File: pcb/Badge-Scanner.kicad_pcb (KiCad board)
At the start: 2 copper layers, 73 x 52 mm, 64 parts, among them J1 NFC-Module, J2 Serial, J3 I2C, J4 Micro_SD_Card_Det1, Q1 AO3400A, Q2 AO3401A, Q3 AO3401A, Q4 AO3401A, Q5 AO3400A, Q6 AO3400A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

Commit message: style: enlarge pin description text
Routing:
- net GND: vias 0 -> 3
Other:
- board text added: "SD-Card (SPI1) 11<DET 12<MISO 13>CS 14<SCK 15>MOSI NFC (SPI0) 16<MISO 17>CS 18>SCK 19>MOSI 20>RST 21<IRQ"
- board text removed: "SD-Card SPI1 11 DETECT 12 MISO 13 CS 14 SCK 15 MOSI NFC SPI0 16 MISO 17 CS 18 SCK 19 MOSI 20 RST 21 IRQ"
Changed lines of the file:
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@@
 	)
 	(gr_text " 0>UART0 TX\n 1<UART0 RX\n 2>LED\n 3>Buzzer\n 4=I2C0 SDA\n 5>I2C0 SCL\n 6<~{Button}\n 8<~{Charge Active}\n 9<~{Charge Standby}\n27>Power Off\n28<Battery Voltage	"
-		(at 164.5 115.75 0)
+		(at 165 118.5 0)
 		(layer "B.SilkS")
 		(effects
 			(font
-				(size 1 1)
+				(size 1.4 1.5)
 				(thickness 0.15)
 			)
@@
 		)
 	)
-	(gr_text "SD-Card SPI1\n11	DETECT\n12	MISO\n13	CS\n14	SCK\n15	MOSI\n\nNFC SPI0\n16	MISO\n17	CS\n18	SCK\n19	MOSI\n20	RST\n21	IRQ"
-		(at 105 115.75 0)
+	(gr_text "SD-Card\n(SPI1)\n11<DET\n12<MISO\n13>CS\n14<SCK\n15>MOSI\n\nNFC \n(SPI0)\n16<MISO\n17>CS\n18>SCK\n19>MOSI\n20>RST\n21<IRQ"
+		(at 104.75 118 0)
 		(layer "B.SilkS")
 		(effects
 			(font
-				(size 1 1)
+				(size 1.4 1.5)
 				(thickness 0.15)
 			)
@@
 		(net 7)
 	)
+	(via
+		(at 120 116.25)
+		(size 0.5)
+		(drill 0.3)
+		(layers "F.Cu" "B.Cu")
+		(free yes)
+		(net 7)
+	)
+	(via
+		(at 130 116.25)
+		(size 0.5)
+		(drill 0.3)
+		(layers "F.Cu" "B.Cu")
+		(free yes)
+		(net 7)
+	)
+	(via
+		(at 125 116.25)
+		(size 0.5)
+		(drill 0.3)
+		(layers "F.Cu" "B.Cu")
+		(free yes)
+		(net 7)
+	)

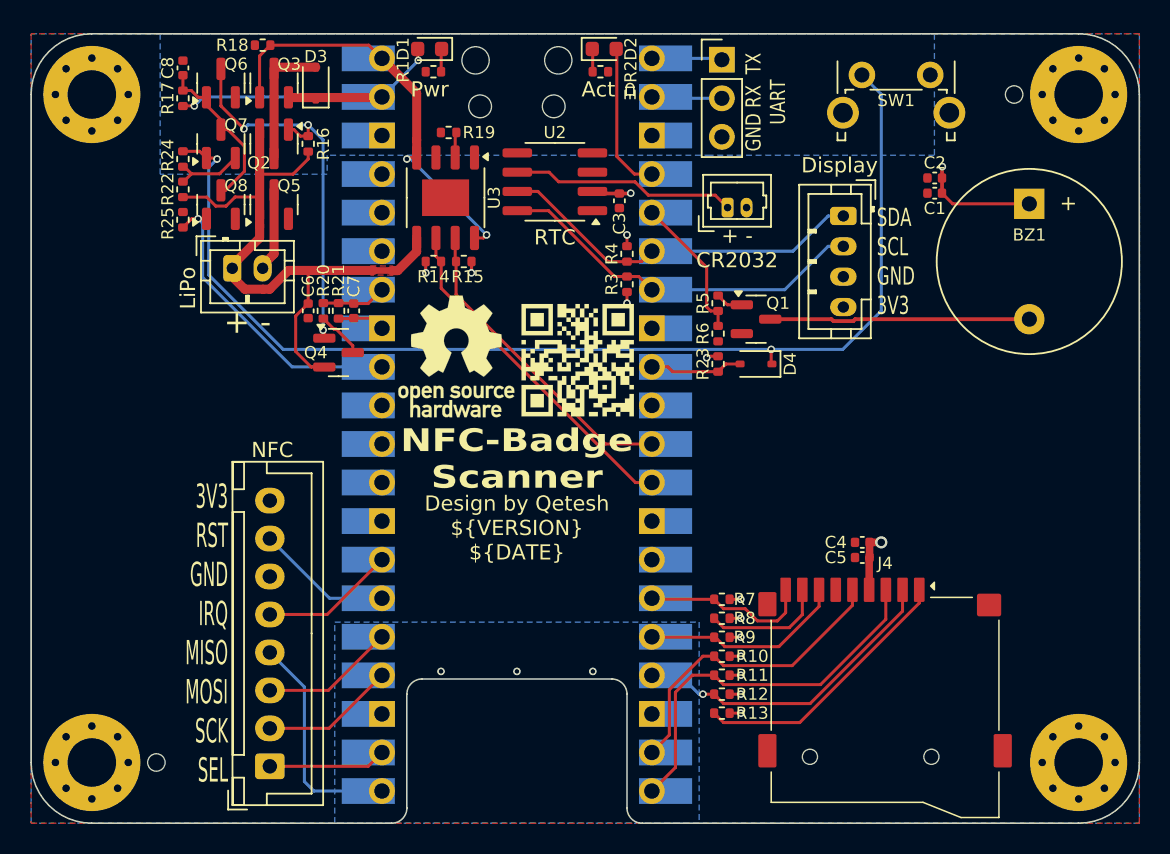
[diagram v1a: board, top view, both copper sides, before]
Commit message: style: silkscreen improvements
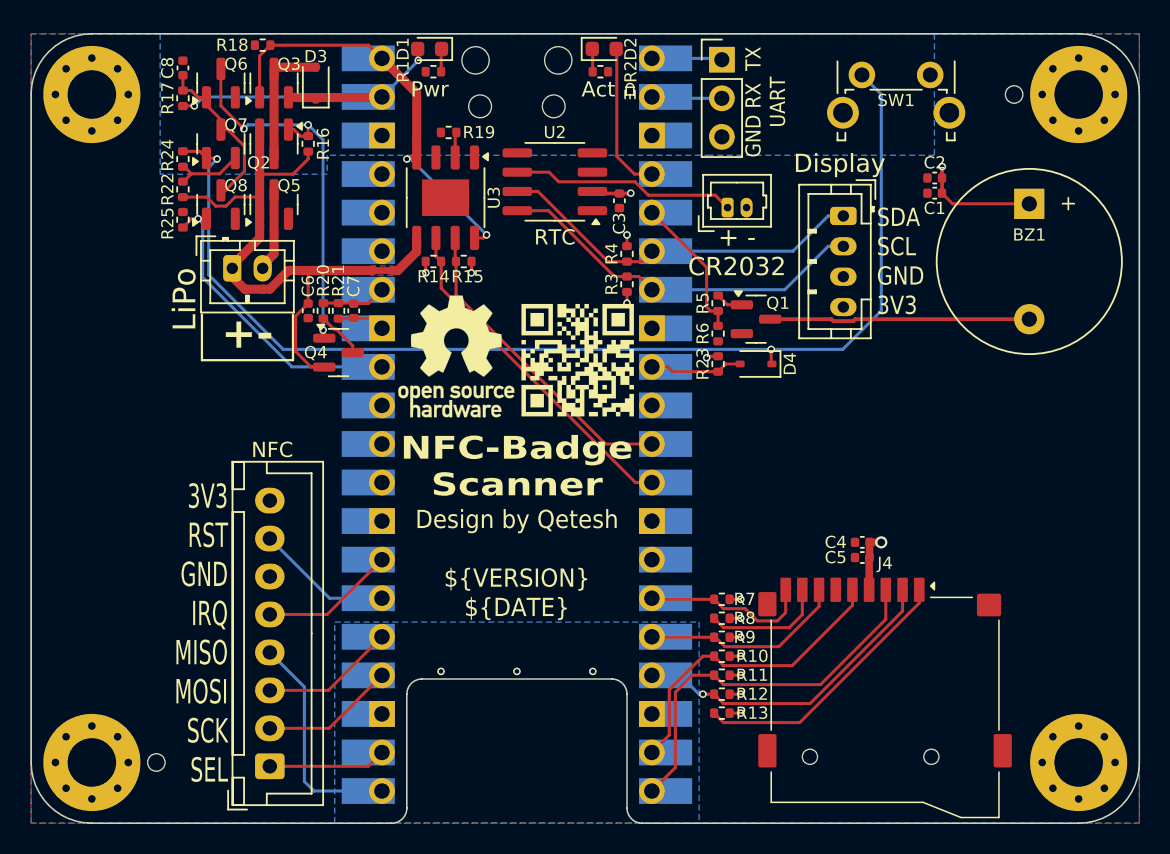
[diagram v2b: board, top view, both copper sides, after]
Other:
- board text added: "+-"
- board text removed: "+ -"
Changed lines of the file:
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@@
 	)
 	(setup
+		(stackup
+			(layer "F.SilkS"
+				(type "Top Silk Screen")
+				(color "White")
+			)
+			(layer "F.Paste"
+				(type "Top Solder Paste")
+			)
+			(layer "F.Mask"
+				(type "Top Solder Mask")
+				(color "Blue")
+				(thickness 0.01)
+			)
+			(layer "F.Cu"
+				(type "copper")
+				(thickness 0.035)
+			)
+			(layer "dielectric 1"
+				(type "core")
+				(color "FR4 natural")
+				(thickness 1.51)
+				(material "FR4")
+				(epsilon_r 4.5)
+				(loss_tangent 0.02)
+			)
+			(layer "B.Cu"
+				(type "copper")
+				(thickness 0.035)
+			)
+			(layer "B.Mask"
+				(type "Bottom Solder Mask")
+				(color "Blue")
+				(thickness 0.01)
+			)
+			(layer "B.Paste"
+				(type "Bottom Solder Paste")
+			)
+			(layer "B.SilkS"
+				(type "Bottom Silk Screen")
+				(color "White")
+			)
+			(copper_finish "None")
+			(dielectric_constraints no)
+		)
 		(pad_to_mask_clearance 0)
 		(allow_soldermask_bridges_in_footprints no)
@@
 		)
 	)
+	(gr_line
+		(start 110.25 95.75)
+		(end 110.25 92.75)
+		(stroke
+			(width 0.15)
+			(type default)
+		)
+		(layer "F.SilkS")
+	)
 	(gr_rect
 		(start 132.2 77.775)
@@
 	)
 	(gr_line
+		(start 104.25 92.75)
+		(end 104.25 95.75)
+		(stroke
+			(width 0.15)
+			(type default)
+		)
+		(layer "F.SilkS")
+	)
+	(gr_line
 		(start 132.125 77.975)
 		(end 132.125 78.525)
@@
 	)
 	(gr_line
+		(start 104.25 95.75)
+		(end 110.25 95.75)
+		(stroke
+			(width 0.15)
+			(type default)
+		)
+		(layer "F.SilkS")
+	)
+	(gr_line
 		(start 97 74.25)
 		(end 162 74.25)
@@
 		(effects
 			(font
-				(size 1 1)
+				(size 1.2 1.2)
 				(thickness 0.15)
 			)
@@
 		(effects
 			(font
-				(size 1.2 0.8)
+				(size 1.2 1)
 				(thickness 0.15)
 			)
@@
 		(effects
 			(font
-				(size 1.6 0.8)
+				(size 1.6 1)
 				(thickness 0.15)
 			)
@@
 		)
 	)
-	(gr_text "+ -"
-		(at 107.25 93.25 0)
+	(gr_text "+-"
+		(at 107.25 94 0)
 		(layer "F.SilkS")
 		(effects
 			(font
-				(size 1.5 1.5)
-				(thickness 0.2)
+				(size 2 2)
+				(thickness 0.4)
+				(bold yes)
 			)
 		)
 	)
-	(gr_text "Design by Qetesh\n${VERSION}\n${DATE}"
-		(at 125 109 0)
+	(gr_text "Design by Qetesh\n\n${VERSION}\n${DATE}"
+		(at 125 112.75 0)
 		(layer "F.SilkS")
 		(effects
 			(font
-				(size 1 1)
+				(size 1.2 1.1)
 				(thickness 0.15)
 			)
@@
 	)
 	(gr_text "+ -\nCR2032"
-		(at 139.5 89.75 0)
+		(at 139.5 86.96 0)
 		(layer "F.SilkS")
 		(effects
 			(font
-				(size 1 1)
+				(size 1.2 1.2)
 				(thickness 0.15)
 			)
-			(justify bottom)
+			(justify top)
 		)
 	)
@@
 		(effects
 			(font
-				(size 1 0.8)
+				(size 1 0.9)
 				(thickness 0.15)
 			)
@@
 	)
 	(gr_text "LiPo"
-		(at 102.75 91 90)
+		(at 104 91.75 90)
 		(layer "F.SilkS")
 		(effects
 			(font
-				(size 1 1)
+				(size 1.5 1.5)
 				(thickness 0.15)
 			)
-			(justify top)
+			(justify bottom)
 		)
 	)
 	(gr_text "NFC-Badge\nScanner"
-		(at 125 102.25 0)
+		(at 125 102.75 0)
 		(layer "F.SilkS")
 		(effects

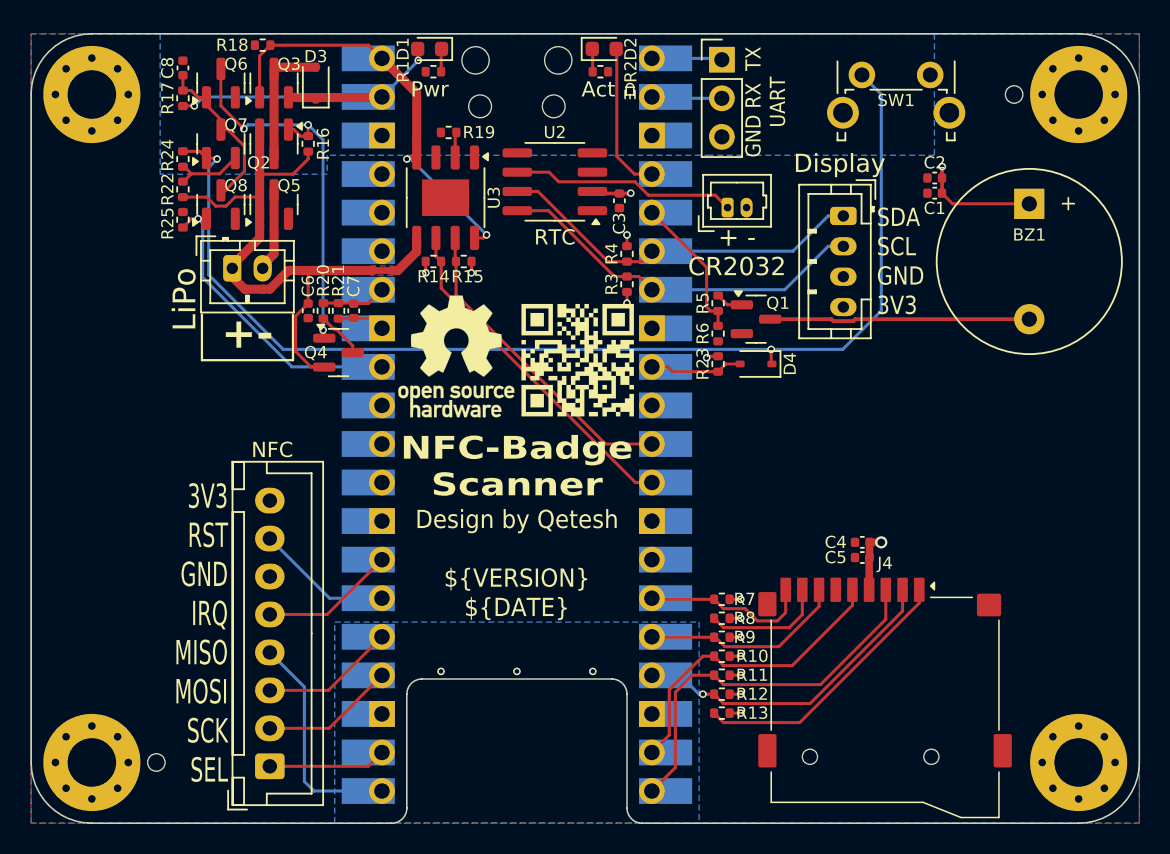
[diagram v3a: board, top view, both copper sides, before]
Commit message: feat: optional fan connector
feat: add 3V reference for ADC
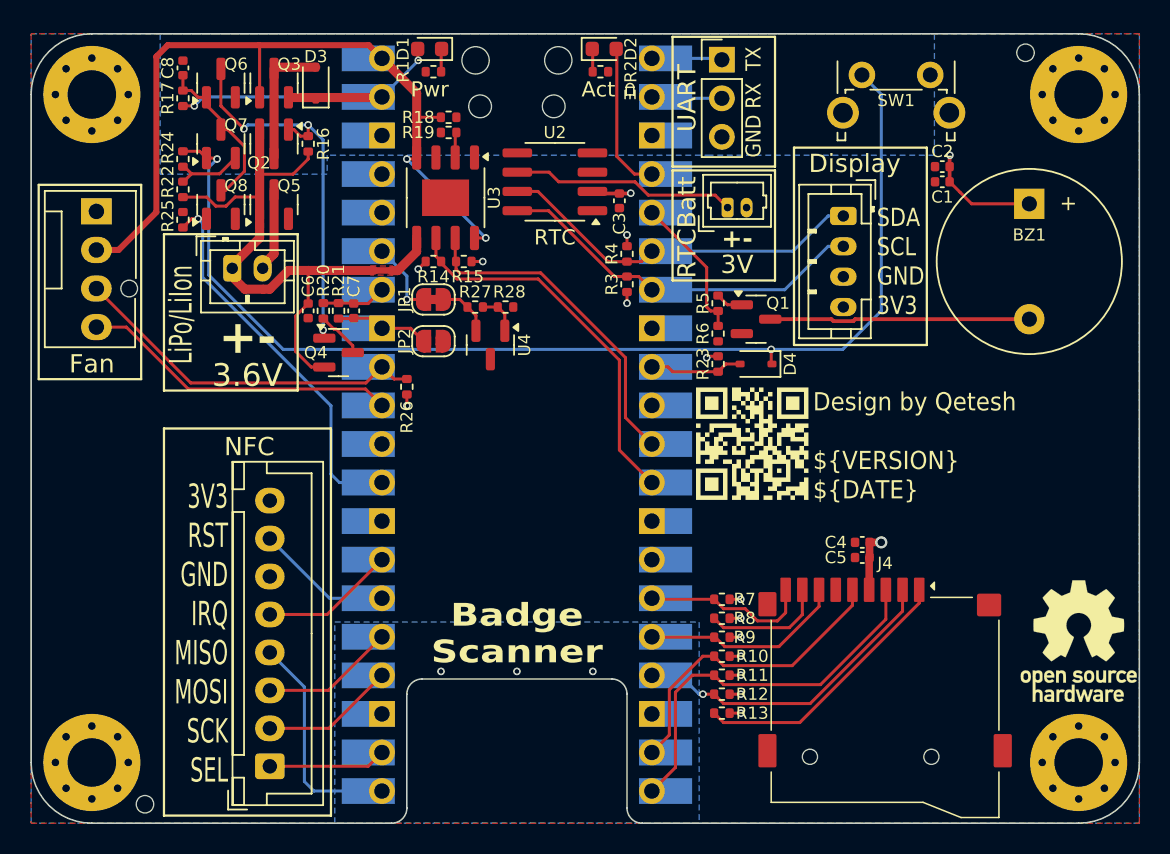
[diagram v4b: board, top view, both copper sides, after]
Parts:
- added JP1: VREF, Jumper:SolderJumper-2_P1.3mm_Bridged_RoundedPad1.0x1.5mm, F.Cu at (119.5, 91.8)
- added JP2: AGND, Jumper:SolderJumper-2_P1.3mm_Open_RoundedPad1.0x1.5mm, F.Cu at (119.5, 94.5)
- added M1: Fan, Connector:FanPinHeader_1x04_P2.54mm_Vertical, F.Cu at (97.3, 86.0)
- added R26: 10k, Resistor_SMD:R_0402_1005Metric, F.Cu at (117.8, 97.5)
- added R27: 2k, Resistor_SMD:R_0402_1005Metric, F.Cu at (122.2, 92.2)
- added R28: 10k, Resistor_SMD:R_0402_1005Metric, F.Cu at (124.2, 92.2)
- added U4: CJ431, Package_TO_SOT_SMD:SOT-23, F.Cu at (123.2, 94.8)
- R3, R4: value 2k2 -> 2k
- moved REF** 45.1 mm to (162.0, 114.2)
- moved R18 13.1 mm to (120.5, 79.8), turned to 0 degrees
- moved G*** 12.7 mm to (140.5, 101.2)
- moved REF** 2.85 mm to (158.5, 75.5)
- moved REF** 2.85 mm to (100.5, 125.0)
- moved C1 0.90 mm to (153.0, 84.0)
- moved C2 0.90 mm to (153.0, 83.0)
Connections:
- U1 pad 29: unconnected-(U1-GP22-Pad29)_1 -> /BattPwrOff
- U1 pad 31: unconnected-(U1-GP26-Pad31) -> /FAN_PWM
- U1 pad 32: /BattPwrOff -> /FAN_TACHO
- U1 pad 35: unconnected-(U1-ADC_VREF-Pad35) -> /ADC_VREF
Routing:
- net VBUS: track 27.8 -> 52.1 mm
- net /FAN_TACHO: track 0.00 -> 23.9 mm
- net /FAN_PWM: track 0.00 -> 20.9 mm
- net /BattPwrOff: track 20.1 -> 25.8 mm
- net /ADC_VREF: track 0.00 -> 4.96 mm, vias 0 -> 1
- net /3V_REF: track 0.00 -> 3.59 mm
- net GNDA: track 3.15 -> 6.24 mm
- net Net-(U4-REF): track 0.00 -> 2.73 mm
- net /~{ChargeStdby}: track 22.6 -> 25.1 mm
- net /~{ChargeActive}: track 20.7 -> 22.1 mm
- net +3V3: track 23.3 -> 23.7 mm, vias 15 -> 16
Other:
- board text added: "0>UART0 TX 1<UART0 RX 2>LED 3>Buzzer 4=I2C0 SDA 5>I2C0 SCL 6<~{Button} 8<~{Charge Active} 9<~{Charge Standby} 22>Power Off 26>Fan PWM 27<Fan Tacho 28<Battery Voltage"
- board text added: "3.6V"
- board text added: "3V"
- board text added: "Badge Scanner"
- board text added: "Fan"
- board text added: "GND RX TX"
- board text added: "LiPo/LiIon"
- board text added: "NFC (SPI0) 16<MISO 17>CS 18>SCK 19>MOSI 20>RST 21<IRQ"
- board text added: "RTCBatt"
- board text added: "SD (SPI1) 11<DET 12<MISO 13>CS 14<SCK 15>MOSI"
- board text added: "UART"
- board text removed: "+ - CR2032"
- board text removed: "0>UART0 TX 1<UART0 RX 2>LED 3>Buzzer 4=I2C0 SDA 5>I2C0 SCL 6<~{Button} 8<~{Charge Active} 9<~{Charge Standby} 27>Power Off 28<Battery Voltage"
- board text removed: "GND RX TX UART"
- board text removed: "LiPo"
- board text removed: "NFC-Badge Scanner"
- board text removed: "SD-Card (SPI1) 11<DET 12<MISO 13>CS 14<SCK 15>MOSI NFC (SPI0) 16<MISO 17>CS 18>SCK 19>MOSI 20>RST 21<IRQ"

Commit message: fix: change resistor values for batt measurement
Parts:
- R20, R21: value 1M -> 100k
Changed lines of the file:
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@@
 			)
 		)
-		(property "Value" "1M"
+		(property "Value" "100k"
 			(at 0 1.17 90)
 			(layer "F.Fab")
@@
 			)
 		)
-		(property "LCSC" "C26083"
+		(property "LCSC" "C25741"
 			(at 0 0 90)
 			(unlocked yes)
@@
 			)
 		)
-		(property "Value" "1M"
+		(property "Value" "100k"
 			(at 0 1.17 90)
 			(layer "F.Fab")
@@
 			)
 		)
-		(property "LCSC" "C26083"
+		(property "LCSC" "C25741"
 			(at 0 0 -90)
 			(unlocked yes)

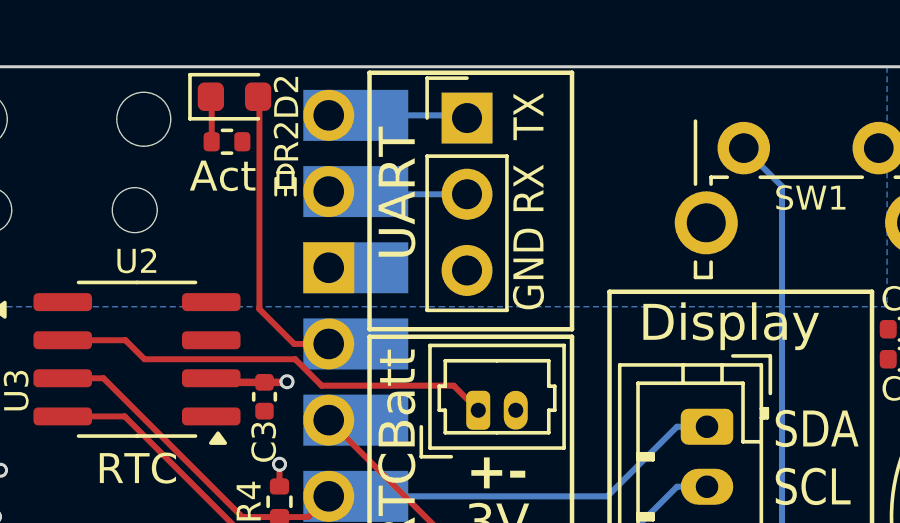
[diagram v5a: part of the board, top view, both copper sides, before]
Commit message: fix: turn around UART connector
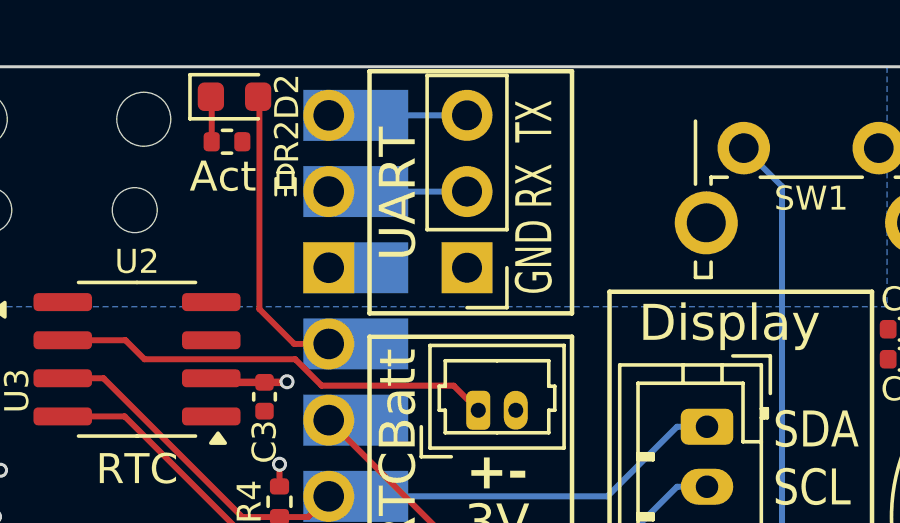
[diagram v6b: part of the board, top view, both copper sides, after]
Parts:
- moved J2 4.99 mm to (138.5, 81.0), turned to 180 degrees
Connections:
- J2 pad 1: /UART0TX -> GND
- J2 pad 3: GND -> /UART0TX
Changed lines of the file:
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@@
 	(footprint "Connector_PinHeader_2.54mm:PinHeader_1x03_P2.54mm_Vertical"
 		(layer "F.Cu")
-		(at 138.5 75.96)
+		(at 138.5 80.95 180)
 		(descr "Through hole straight pin header, 1x03, 2.54mm pitch, single row")
 		(tags "Through hole pin header THT 1x03 2.54mm single row")
 		(property "Reference" "J2"
-			(at 0 -2.33 0)
+			(at 0 -2.33 360)
 			(layer "F.SilkS")
 			(hide yes)
@@
 		)
 		(property "Value" "Serial"
-			(at 0 7.41 0)
+			(at 0 7.41 360)
 			(layer "F.Fab")
 			(effects
@@
 		)
 		(property "Footprint" "Connector_PinHeader_2.54mm:PinHeader_1x03_P2.54mm_Vertical"
-			(at 0 0 0)
+			(at 0 0 180)
 			(unlocked yes)
 			(layer "F.Fab")
@@
 		)
 		(property "Datasheet" ""
-			(at 0 0 0)
+			(at 0 0 180)
 			(unlocked yes)
 			(layer "F.Fab")
@@
 		)
 		(property "Description" "Generic connector, single row, 01x03, script generated (kicad-library-utils/schlib/autogen/connector/)"
-			(at 0 0 0)
+			(at 0 0 180)
 			(unlocked yes)
 			(layer "F.Fab")
@@
 		(attr through_hole dnp)
 		(fp_line
-			(start -1.33 -1.33)
-			(end 0 -1.33)
+			(start 1.33 1.27)
+			(end 1.33 6.41)
 			(stroke
 				(width 0.12)
@@
 		)
 		(fp_line
-			(start -1.33 0)
-			(end -1.33 -1.33)
+			(start -1.33 6.41)
+			(end 1.33 6.41)
 			(stroke
 				(width 0.12)
@@
 		(fp_line
 			(start -1.33 1.27)
-			(end -1.33 6.41)
+			(end 1.33 1.27)
 			(stroke
 				(width 0.12)
@@
 		(fp_line
 			(start -1.33 1.27)
-			(end 1.33 1.27)
+			(end -1.33 6.41)
 			(stroke
 				(width 0.12)
@@
 		)
 		(fp_line
-			(start -1.33 6.41)
-			(end 1.33 6.41)
+			(start -1.33 0)
+			(end -1.33 -1.33)
 			(stroke
 				(width 0.12)
@@
 		)
 		(fp_line
-			(start 1.33 1.27)
-			(end 1.33 6.41)
+			(start -1.33 -1.33)
+			(end 0 -1.33)
 			(stroke
 				(width 0.12)
@@
 		)
 		(fp_line
-			(start -1.8 -1.8)
-			(end -1.8 6.85)
+			(start 1.8 6.85)
+			(end 1.8 -1.8)
 			(stroke
 				(width 0.05)
@@
 		)
 		(fp_line
-			(start -1.8 6.85)
-			(end 1.8 6.85)
+			(start 1.8 -1.8)
+			(end -1.8 -1.8)
 			(stroke
 				(width 0.05)
@@
 		)
 		(fp_line
-			(start 1.8 -1.8)
-			(end -1.8 -1.8)
+			(start -1.8 6.85)
+			(end 1.8 6.85)
 			(stroke
 				(width 0.05)
@@
 		)
 		(fp_line
-			(start 1.8 6.85)
-			(end 1.8 -1.8)
+			(start -1.8 -1.8)
+			(end -1.8 6.85)
 			(stroke
 				(width 0.05)
@@
 		)
 		(fp_line
-			(start -1.27 -0.635)
-			(end -0.635 -1.27)
+			(start 1.27 6.35)
+			(end -1.27 6.35)
 			(stroke
 				(width 0.1)
@@
 		)
 		(fp_line
-			(start -1.27 6.35)
-			(end -1.27 -0.635)
+			(start 1.27 -1.27)
+			(end 1.27 6.35)
 			(stroke
 				(width 0.1)
@@
 		)
 		(fp_line
-			(start 1.27 -1.27)
-			(end 1.27 6.35)
+			(start -1.27 6.35)
+			(end -1.27 -0.635)
 			(stroke
 				(width 0.1)
@@
 		)
 		(fp_line
-			(start 1.27 6.35)
-			(end -1.27 6.35)
+			(start -1.27 -0.635)
+			(end -0.635 -1.27)
 			(stroke
 				(width 0.1)
@@
 		)
 		(pad "1" thru_hole rect
-			(at 0 0)
+			(at 0 0 180)
 			(size 1.7 1.7)
 			(drill 1)
 			(layers "*.Cu" "*.Mask")
 			(remove_unused_layers no)
-			(net 31 "/UART0TX")
+			(net 7 "GND")
 			(pinfunction "Pin_1")
 			(pintype "passive")
 		)
 		(pad "2" thru_hole oval
-			(at 0 2.54)
+			(at 0 2.54 180)
 			(size 1.7 1.7)
 			(drill 1)
@@
 		)
 		(pad "3" thru_hole oval
-			(at 0 5.08)
+			(at 0 5.08 180)
 			(size 1.7 1.7)
 			(drill 1)
 			(layers "*.Cu" "*.Mask")
 			(remove_unused_layers no)
-			(net 7 "GND")
+			(net 31 "/UART0TX")
 			(pinfunction "Pin_3")
 			(pintype "passive")
@@
 	)
 	(gr_rect
-		(start 135.25 74.45)
-		(end 142 83)
+		(start 135.25 74.4)
+		(end 142 82.47)
 		(stroke
 			(width 0.15)
@@
 	)
 	(gr_text "GND RX  TX"
-		(at 140 78.75 90)
+		(at 140.05 78.6 90)
 		(layer "F.SilkS")
 		(effects
 			(font
-				(size 1 0.9)
+				(size 1.2 0.8)
 				(thickness 0.15)
 			)
@@
 	(segment
 		(start 133.89 75.87)
-		(end 138.41 75.87)
+		(end 138.5 75.87)
 		(width 0.2)
 		(layer "B.Cu")
@@
 	)
 	(segment
-		(start 138.41 75.87)
-		(end 138.5 75.96)
-		(width 0.2)
-		(layer "B.Cu")
-		(net 31)
-	)
-	(segment
-		(start 135.25 78.5)
-		(end 138.5 78.5)
-		(width 0.2)
-		(layer "B.Cu")
-		(net 32)
-	)
-	(segment
 		(start 133.89 78.41)
-		(end 135.16 78.41)
-		(width 0.2)
-		(layer "B.Cu")
-		(net 32)
-	)
-	(segment
-		(start 135.16 78.41)
-		(end 135.25 78.5)
+		(end 138.5 78.41)
 		(width 0.2)
 		(layer "B.Cu")

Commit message: fix: move power LED to 3.3V rail
VSYS is too unstable since its voltage changes a lot between usb and battery powered mode
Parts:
- added G***: LOGO, My_Footprints:CutieMark5mmInverted, F.Cu at (162.0, 106.2)
- R1: value 1k5 -> 680R
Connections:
- D1 pad 2: VSYS -> +3V3
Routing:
- net VSYS: track 23.7 -> 19.5 mm, vias 2 -> 1
- net +3V3: track 23.7 -> 24.5 mm, vias 16 -> 17
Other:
- board text added: "qete.sh/el"
